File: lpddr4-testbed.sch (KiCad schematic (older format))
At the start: 43 parts, among them J1 ddr4-sodimm-edge-connector, U1 MT53E256M16D1

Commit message: Introduce schematic sheets
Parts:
- removed C1: C_100p_0402, lpddr4-testbed-footprints:0402-cap, symbol lpddr4-testbed:C_100p_0402
- removed C2: C_3p3_0402, lpddr4-testbed-footprints:0402-res, symbol lpddr4-testbed:C_3p3_0402
- removed C3: C_10n_0402, lpddr4-testbed-footprints:0402-cap, symbol lpddr4-testbed:C_10n_0402
- removed C4: C_100n_0402_6V3, lpddr4-testbed-footprints:0402-cap, symbol lpddr4-testbed:C_100n_0402_6V3
- removed J1: ddr4-sodimm-edge-connector, lpddr4-testbed-footprints:SODIMM_DDR4_EDGE, symbol lpddr4-testbed:ddr4-sodimm-edge-connector
- removed R1: R_240R_0402, lpddr4-testbed-footprints:0402-res, symbol lpddr4-testbed:R_240R_0402
- removed R10: R_75R_0402, lpddr4-testbed-footprints:0402-res, symbol lpddr4-testbed:R_75R_0402
- removed R11, R12, R27, R28, R29, R3, R31, R36, R4, R5: R_0R_0402, lpddr4-testbed-footprints:0402-res, symbol lpddr4-testbed:R_0R_0402
- removed R13, R14, R15, R16, R17, R18, R19, R20, R21, R22, R23, R24, R25, R26, R30, R32, R37, R6, R7, R8, R9: R_40R2_0402, lpddr4-testbed-footprints:0402-res, symbol lpddr4-testbed:R_40R2_0402
- removed R2: R_120R_0402, lpddr4-testbed-footprints:0402-res, symbol lpddr4-testbed:R_120R_0402
- removed R33, R34: R_80R6_0402, lpddr4-testbed-footprints:0402-res, symbol lpddr4-testbed:R_80R6_0402
- removed R35: R_4k7_0402, lpddr4-testbed-footprints:0402-res, symbol lpddr4-testbed:R_4k7_0402
- removed U1: MT53E256M16D1, lpddr4-testbed-footprints:BGA-200_10.0x14.5mm_Layout12x22_P0.80x0.65mm, symbol lpddr4-testbed:MT53E256M16D1
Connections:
- net labels removed: ACT_N, ALERT_N, BA0, BA1, BG0, BG1, CA0_A, CA0_B, CA1_A, CA1_B, CA2_A, CA2_B, CA3_A, CA3_B, CA4_A, CA4_B, CA5_A, CA5_B, CK0_C, CK0_T, CK1_C, CK1_T, CKE0_A, CKE0_B, CKE_0, CKE_0_A, CKE_0_B, CKE_1, CS0_N, CS0_N_A, CS0_N_B, CS_0_N, CS_1_N, DDRVCC, DM0_N, DM1_N, DM2_N, DM3_N, DQ00, DQ01, DQ02, DQ03, DQ04, DQ05, DQ06, DQ07, DQ08, DQ09, DQ10, DQ11, DQ12, DQ13, DQ14, DQ15, DQ16, DQ17, DQ18, DQ19, DQ20, DQ21, DQ22, DQ23, DQ24, DQ25, DQ26, DQ27, DQ28, DQ29, DQ30, DQ31, DQS0_C, DQS0_T, DQS1_C, DQS1_T, DQS2_C, DQS2_T, DQS3_C, DQS3_T, EVENT_N, GND, MEMRST_N, ODT0, ODT0_A, ODT0_B, ODT1, PARITY, RESET_CONN_N, SA0, SA1, SCL, SDA, VDDSPD, VPP, VREFCA, VTT
- wire segments 511 -> 0
- no-connect marks 65 -> 0
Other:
- note added: "LPDDR4 testbed"
- note removed: "Bank adress"
- note removed: "Bank group\n"
- note removed: "Connector"
- note removed: "DDR4"
- note removed: "LPDDR4"
- note removed: "OR"
- note removed: "Pull up or pull down?\n"
- note removed: "Second LPDDR4 die"
- note removed: "Single LPDDR4 die"
- note removed: "To check"
- note removed: "What is taht pin?"
- note removed: "What is this resistor for?"

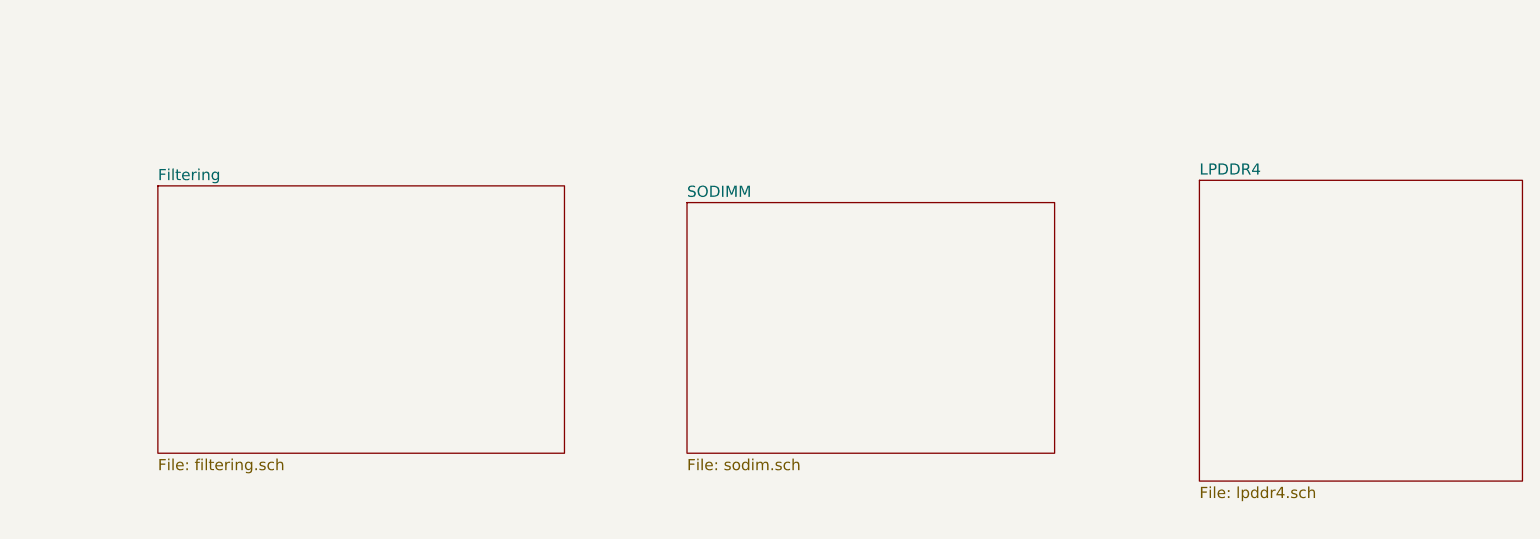
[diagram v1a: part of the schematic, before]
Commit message: Fully routed, DRC clean
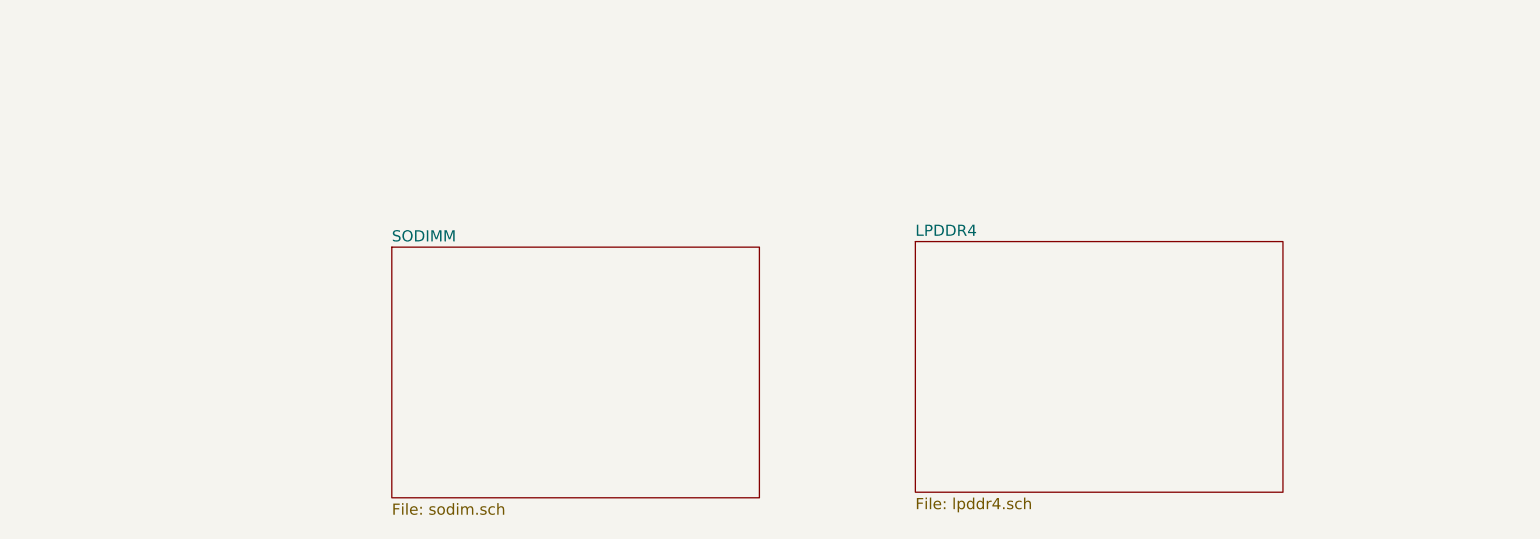
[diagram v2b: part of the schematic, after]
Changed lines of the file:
@@
 $Descr A3 16535 11693
 encoding utf-8
-Sheet 1 4
+Sheet 1 3
 Title ""
 Date ""
@@
 $EndDescr
 $Sheet
-S 5225 5000 1825 1200
-U 5FD72AB0
-F0 "Filtering" 50
-F1 "filtering.sch" 50
-$EndSheet
-$Sheet
-S 7600 5075 1650 1125
+S 6275 5275 1650 1125
 U 5FDC4A05
 F0 "SODIMM" 50
 F1 "sodim.sch" 50
 $EndSheet
+Text Notes 725  850  0    98   ~ 20
+LPDDR4 testbed
 $Sheet
-S 9900 4975 1450 1350
-U 5FDC4A45
+S 8625 5250 1650 1125
+U 5FF943AC
 F0 "LPDDR4" 50
 F1 "lpddr4.sch" 50
 $EndSheet
-Text Notes 725  850  0    98   ~ 20
-LPDDR4 testbed
 $EndSCHEMATC

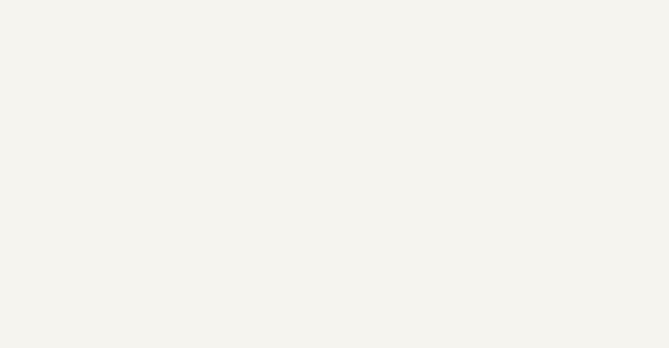
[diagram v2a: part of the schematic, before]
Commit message: Optimize pairs of buried vias
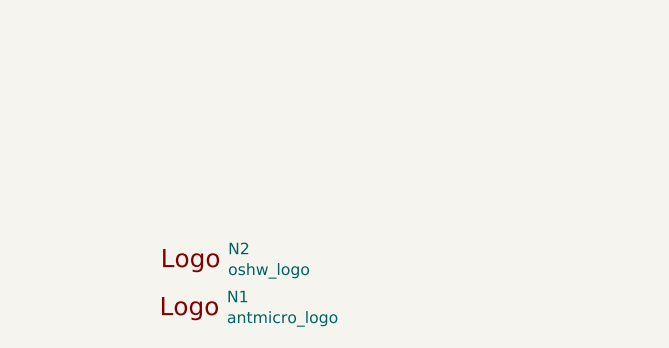
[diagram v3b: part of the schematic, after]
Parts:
- added N1: antmicro_logo, antmicro-footprints:antmicro-logo_scaled_20mm, symbol antmicroMechanicalParts:antmicro_logo
- added N2: oshw_logo, antmicro-footprints:oshw-logo, symbol antmicroMechanicalParts:oshw_logo
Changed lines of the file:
@@
 encoding utf-8
 Sheet 1 3
-Title ""
+Title "LPDDR4 testbed"
 Date ""
-Rev ""
+Rev "1.0.0"
 Comp ""
 Comment1 ""
@@
 F1 "lpddr4.sch" 50
 $EndSheet
+$Comp
+L antmicroMechanicalParts:oshw_logo N2
+U 1 1 5FFF48FB
+P 1450 10250
+F 0 "N2" H 1644 10253 50  0000 L CNN
+F 1 "oshw_logo" H 1644 10162 50  0000 L CNN
+F 2 "antmicro-footprints:oshw-logo" H 1470 10010 50  0001 C CNN
+F 3 "" H 1450 10250 50  0001 C CNN
+	1    1450 10250
+	1    0    0    -1
+$EndComp
+$Comp
+L antmicroMechanicalParts:antmicro_logo N1
+U 1 1 5FFF4C1F
+P 1425 10550
+F 0 "N1" H 1639 10643 50  0000 L CNN
+F 1 "antmicro_logo" H 1639 10552 50  0000 L CNN
+F 2 "antmicro-footprints:antmicro-logo_scaled_20mm" H 1325 10800 50  0001 C CNN
+F 3 "" H 1425 10900 50  0001 C CNN
+	1    1425 10550
+	1    0    0    -1
+$EndComp
 $EndSCHEMATC

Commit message: Update local libs, resolve DRC
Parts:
- N1: footprint antmicro-footprints:antmicro-logo_scaled_20mm -> lpddr4-testbed-footprints:antmicro-logo_scaled_20mm; symbol antmicroMechanicalParts:antmicro_logo -> lpddr4-testbed:antmicro_logo
- N2: footprint antmicro-footprints:oshw-logo -> lpddr4-testbed-footprints:oshw-logo; symbol antmicroMechanicalParts:oshw_logo -> lpddr4-testbed:oshw_logo
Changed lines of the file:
@@
 $EndSheet
 $Comp
-L antmicroMechanicalParts:oshw_logo N2
+L lpddr4-testbed:oshw_logo N2
 U 1 1 5FFF48FB
 P 1450 10250
 F 0 "N2" H 1644 10253 50  0000 L CNN
 F 1 "oshw_logo" H 1644 10162 50  0000 L CNN
-F 2 "antmicro-footprints:oshw-logo" H 1470 10010 50  0001 C CNN
+F 2 "lpddr4-testbed-footprints:oshw-logo" H 1470 10010 50  0001 C CNN
 F 3 "" H 1450 10250 50  0001 C CNN
 	1    1450 10250
@@
 $EndComp
 $Comp
-L antmicroMechanicalParts:antmicro_logo N1
+L lpddr4-testbed:antmicro_logo N1
 U 1 1 5FFF4C1F
 P 1425 10550
 F 0 "N1" H 1639 10643 50  0000 L CNN
 F 1 "antmicro_logo" H 1639 10552 50  0000 L CNN
-F 2 "antmicro-footprints:antmicro-logo_scaled_20mm" H 1325 10800 50  0001 C CNN
+F 2 "lpddr4-testbed-footprints:antmicro-logo_scaled_20mm" H 1325 10800 50  0001 C CNN
 F 3 "" H 1425 10900 50  0001 C CNN
 	1    1425 10550

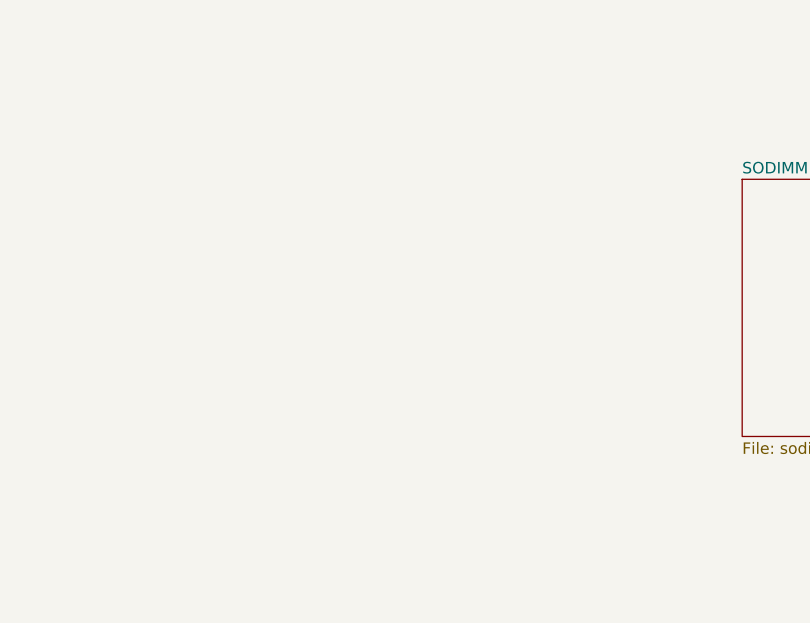
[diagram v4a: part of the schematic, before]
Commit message: Added sheet for EEPROM/LEDs
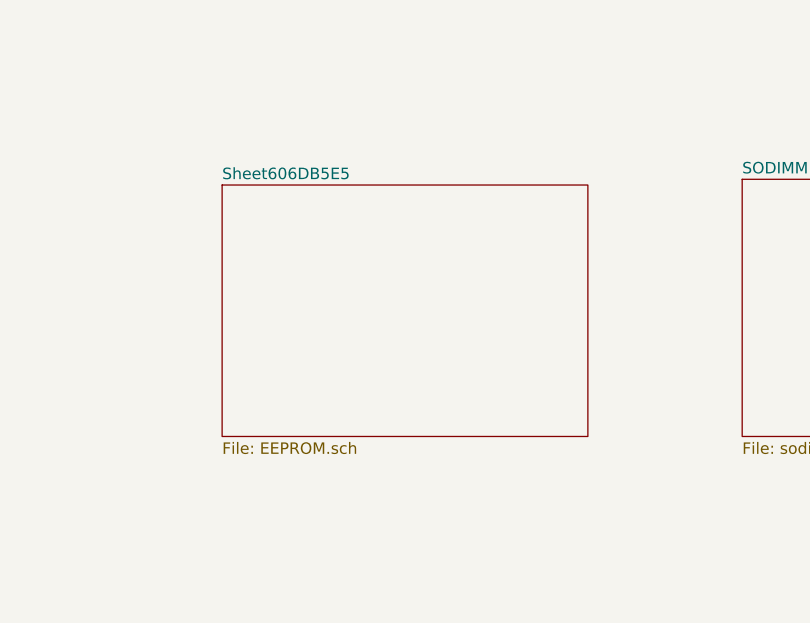
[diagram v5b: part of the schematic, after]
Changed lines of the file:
@@
 $Descr A3 16535 11693
 encoding utf-8
-Sheet 1 3
+Sheet 1 4
 Title "LPDDR4 testbed"
 Date ""
@@
 	1    0    0    -1
 $EndComp
+$Sheet
+S 4000 5300 1600 1100
+U 606DB5E6
+F0 "Sheet606DB5E5" 50
+F1 "EEPROM.sch" 50
+$EndSheet
 $EndSCHEMATC
